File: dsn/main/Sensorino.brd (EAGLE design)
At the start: 100 x 80 mm, 45 parts, among them IC1 LDO3V3

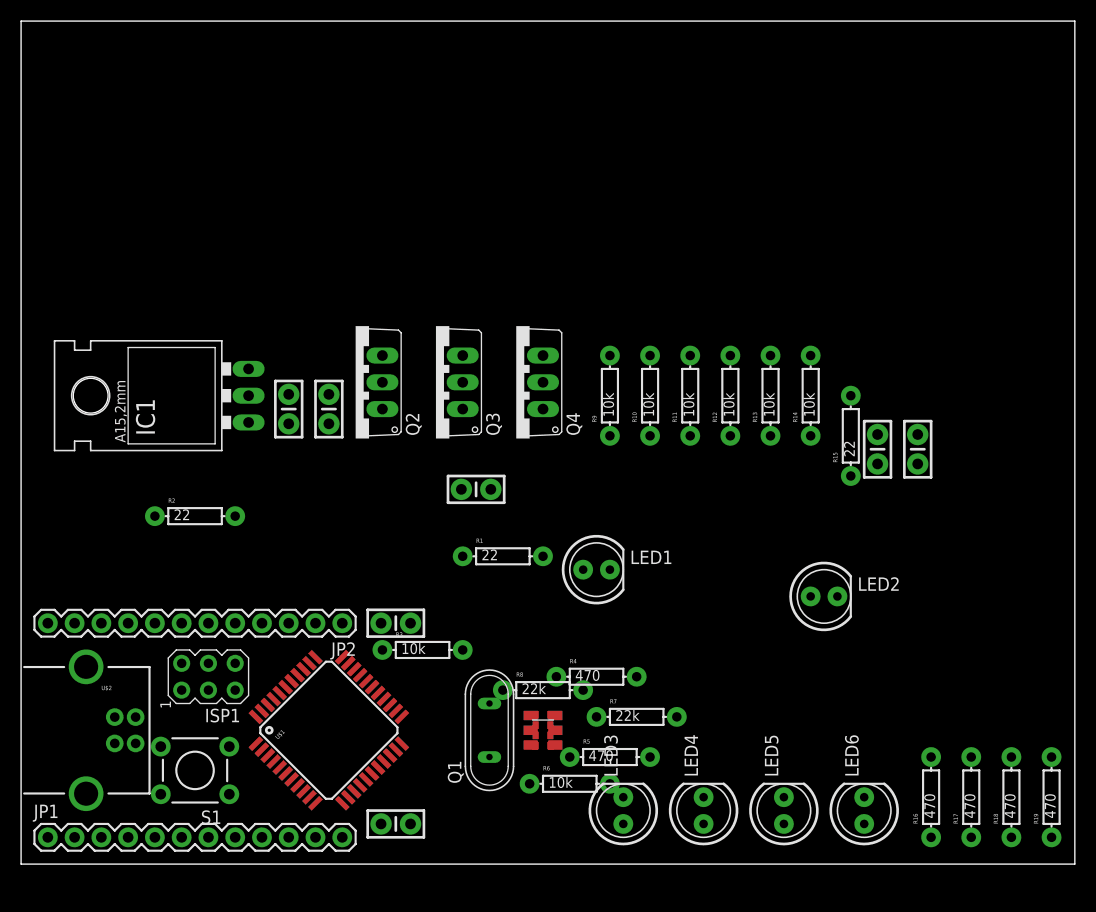
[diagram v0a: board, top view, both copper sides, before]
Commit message: Added PTH render
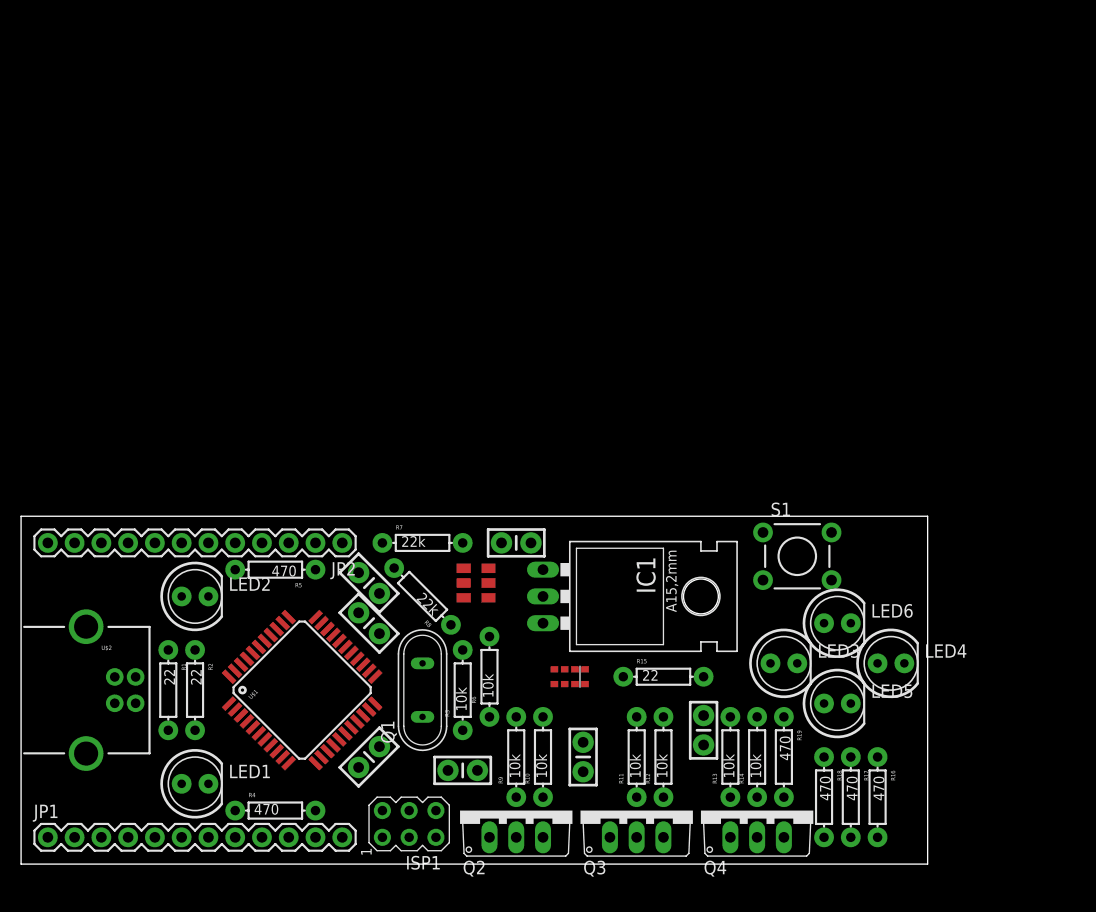
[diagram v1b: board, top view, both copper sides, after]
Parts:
- Q1: value (none) -> 16Mhz
- moved S1 60.7 mm to (73.7, 29.2), turned to 0 degrees
- moved LED2 59.7 mm to (16.5, 25.4)
- moved Q4 46.6 mm to (69.8, 5.08), turned to 0 degrees
- moved Q3 44.9 mm to (58.4, 5.08), turned to 0 degrees
- moved Q2 43.4 mm to (47.0, 5.08), turned to 0 degrees
- moved LED1 43.2 mm to (16.5, 7.62)
- moved C7 43.1 mm to (53.3, 10.2), turned to 270 degrees
- moved IC1 40.3 mm to (53.3, 25.4), turned to 270 degrees
- moved C5 36.6 mm to (41.9, 8.89), turned to 180 degrees
- moved R5 36.4 mm to (24.1, 27.9), turned to 180 degrees
- moved R10 35.8 mm to (49.5, 10.2)
- moved R9 35.4 mm to (47.0, 10.2)
- moved R12 34.9 mm to (61.0, 10.2)
- moved R11 34.7 mm to (58.4, 10.2)
- moved R14 34.7 mm to (69.8, 10.2)
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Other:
- board size 100 x 80 mm -> 86 x 33 mm

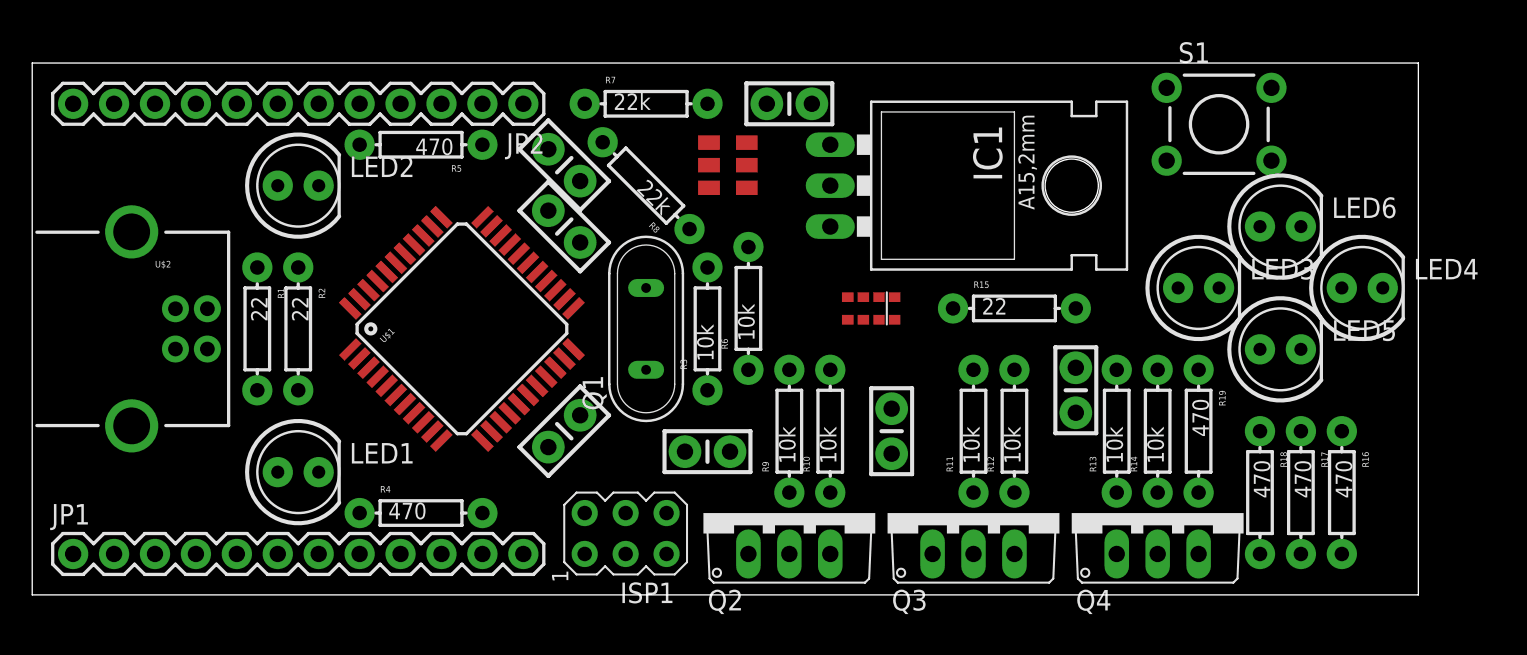
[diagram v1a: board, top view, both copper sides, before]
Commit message: Mosfet changed to a more-acceptable model
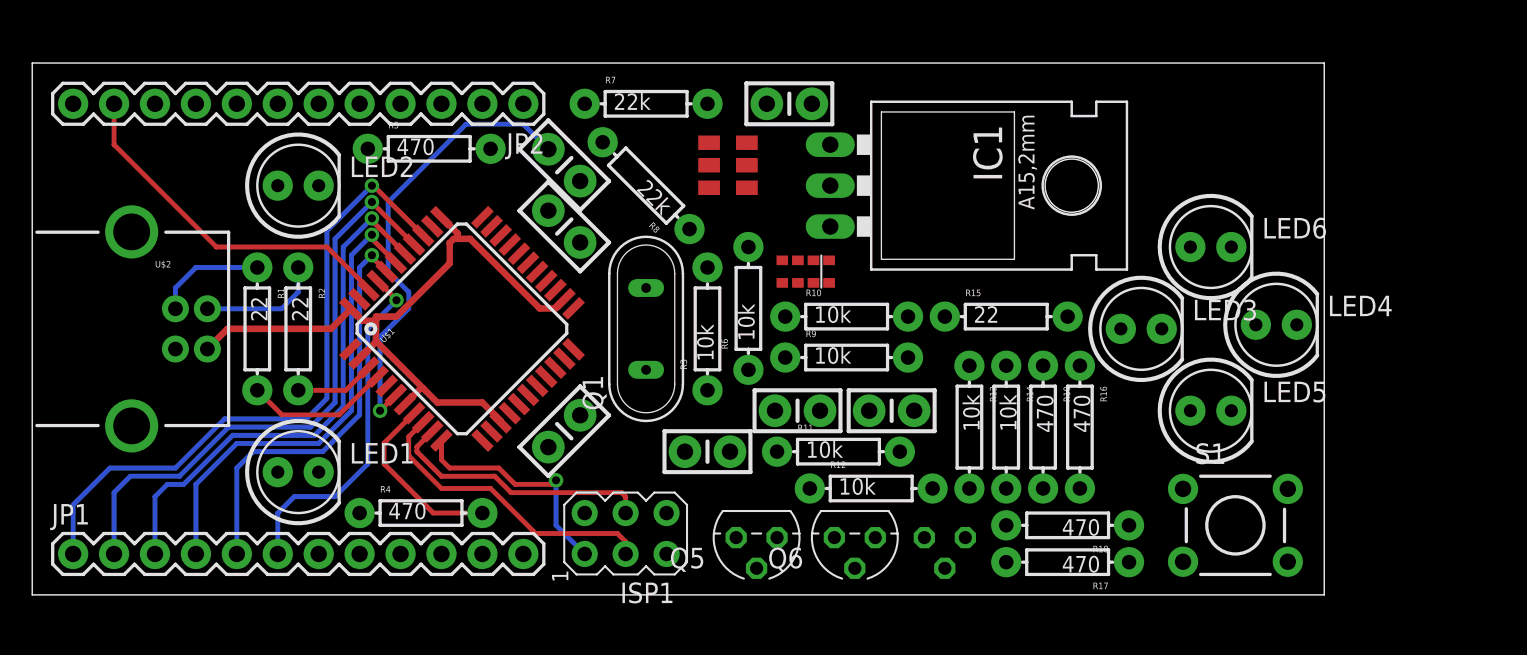
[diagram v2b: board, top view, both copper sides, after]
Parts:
- removed Q2, Q3, Q4: (no value), adafruit:TO220V
- added Q5, Q6, Q7: BSS101, transistor-fet:TO92
- moved S1 24.9 mm to (74.7, 4.32)
- moved R16 16.8 mm to (65.0, 10.4)
- moved R17 15.1 mm to (64.3, 2.03), turned to 180 degrees
- moved R18 12.1 mm to (64.3, 4.32), turned to 180 degrees
- moved C6 11.5 mm to (53.3, 11.4), turned to 180 degrees
- moved R19 9.66 mm to (62.7, 10.4)
- moved R12 9.57 mm to (52.1, 6.60), turned to 0 degrees
- moved R14 9.40 mm to (60.5, 10.4), turned to 270 degrees
- moved R13 9.15 mm to (58.2, 10.4), turned to 270 degrees
- moved R11 8.48 mm to (50.0, 8.89), turned to 0 degrees
- moved R10 7.18 mm to (50.5, 17.3), turned to 0 degrees
- moved C7 5.98 mm to (47.5, 11.4), turned to 180 degrees
- moved LED4 5.80 mm to (77.2, 16.8)
- moved R9 5.79 mm to (50.5, 14.7), turned to 0 degrees
- moved LED5 5.76 mm to (73.2, 11.4)
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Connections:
- net 3V3_PWR: now also Q5.2, Q6.2, Q7.2; no longer Q2.1, Q3.1, Q4.1
- net A1: now also Q5.1; no longer Q2.3
- net A2: now also Q6.1; no longer Q4.3
- net A3: now also Q7.1; no longer Q3.3
- net B1: now also Q5.3; no longer Q2.2
- net B2: now also Q6.3; no longer Q4.2
- net B3: now also Q7.3; no longer Q3.2
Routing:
- net 5V: track 0.00 -> 44.5 mm
- net N$13: track 0.00 -> 40.4 mm, vias 0 -> 1
- net N$14: track 0.00 -> 37.0 mm, vias 0 -> 1
- net N$15: track 0.00 -> 33.0 mm, vias 0 -> 1
- net N$16: track 0.00 -> 29.7 mm, vias 0 -> 1
- net N$6: track 0.00 -> 28.2 mm, vias 0 -> 1
- net N$17: track 0.00 -> 26.0 mm, vias 0 -> 1
- net AREF_SIG: track 0.00 -> 22.1 mm
- net N$18: track 0.00 -> 22.0 mm, vias 0 -> 1
- net SCK_SIG: track 0.00 -> 18.9 mm
- net MOSI_SIG: track 0.00 -> 16.8 mm
- net MISO_SIG: track 0.00 -> 14.4 mm, vias 0 -> 1
- net RXL_SIG: track 0.00 -> 11.3 mm
- net N$2: track 0.00 -> 9.08 mm
- net N$4: track 0.00 -> 7.59 mm
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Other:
- board size 86 x 33 mm -> 80.2 x 33 mm

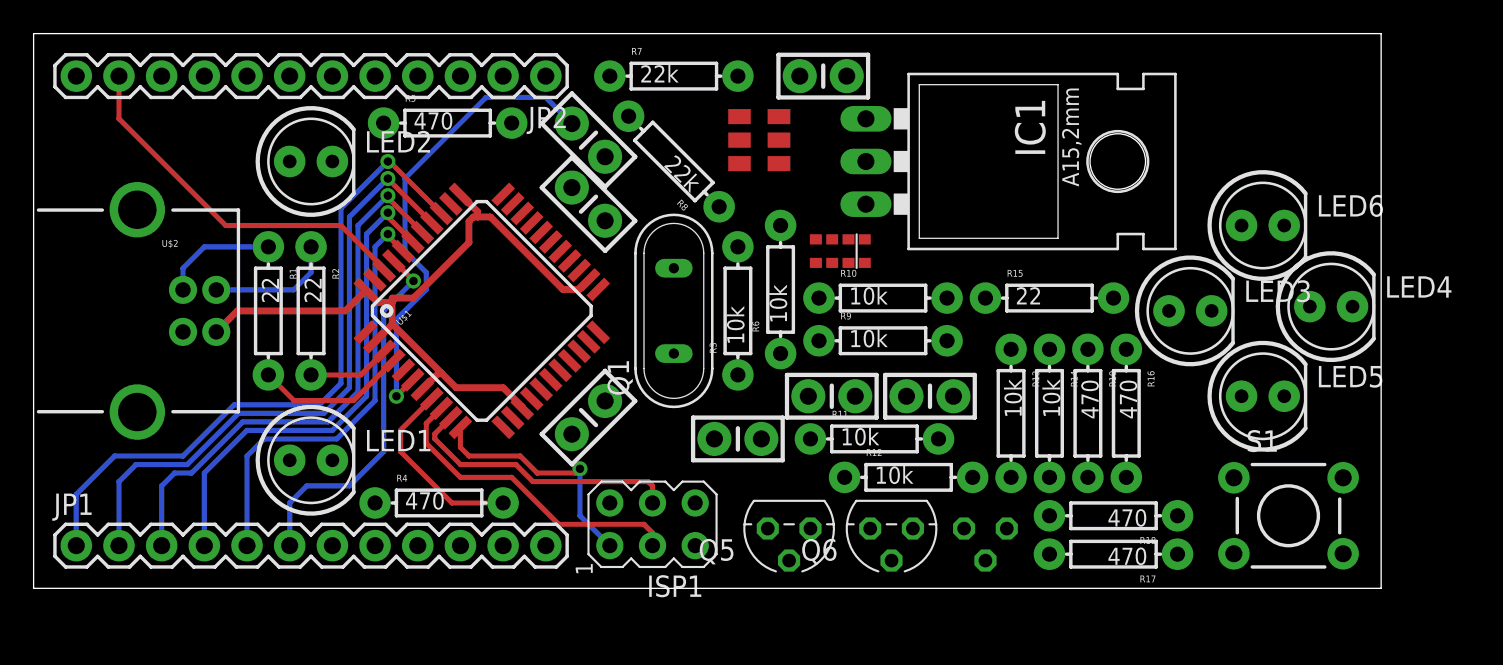
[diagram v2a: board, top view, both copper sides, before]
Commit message: Modified PTH PCB Layout
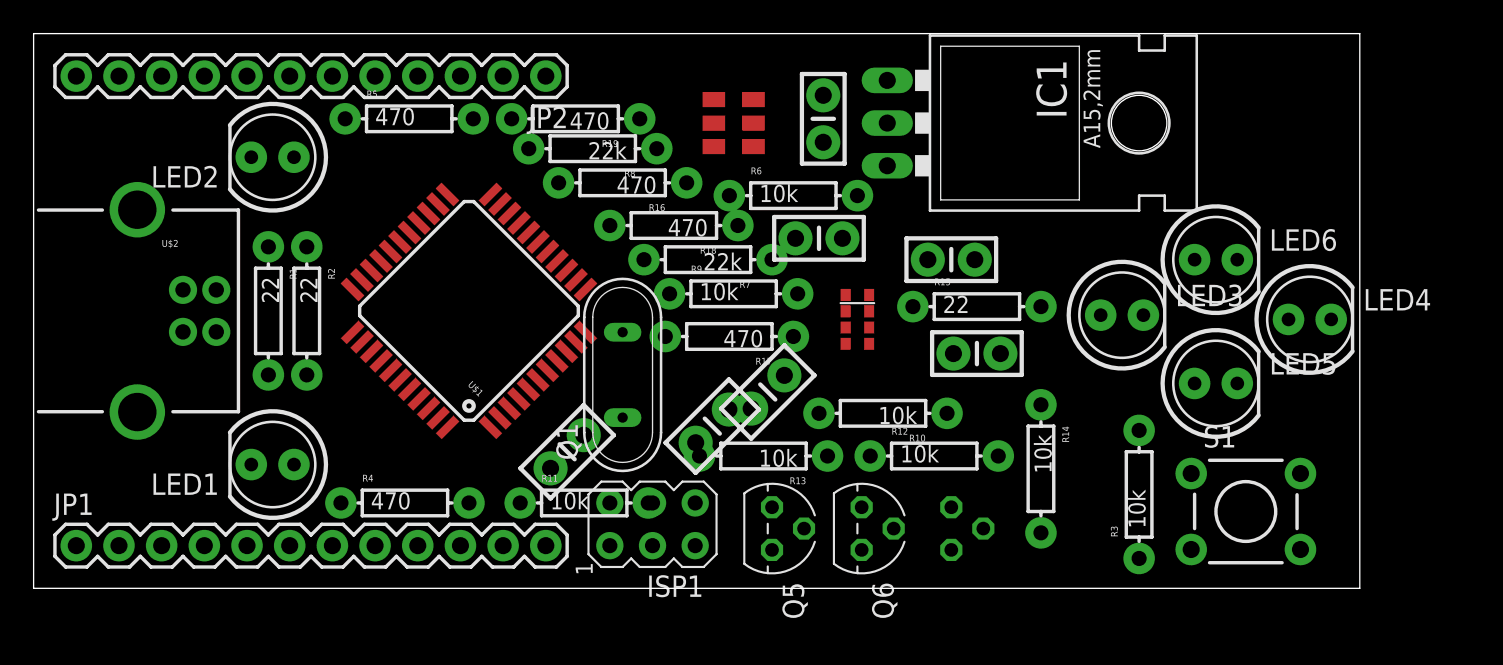
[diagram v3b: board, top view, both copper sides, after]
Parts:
- moved R19 35.2 mm to (32.3, 27.9), turned to 180 degrees
- moved R16 33.0 mm to (35.1, 24.1), turned to 180 degrees
- moved R18 31.3 mm to (38.1, 21.6)
- moved R17 26.3 mm to (41.4, 15.0)
- moved R3 26.3 mm to (65.8, 5.59)
- moved C1 18.5 mm to (40.4, 9.65), turned to 225 degrees
- moved R11 17.7 mm to (32.8, 5.08)
- moved C5 16.6 mm to (54.6, 19.6)
- moved C3 15.5 mm to (43.7, 11.7), turned to 45 degrees
- moved R13 14.9 mm to (43.4, 7.87), turned to 180 degrees
- moved R7 11.1 mm to (40.1, 19.6), turned to 180 degrees
- moved C7 9.43 mm to (46.7, 20.8)
- moved R9 9.32 mm to (41.7, 17.5)
- moved R10 6.86 mm to (50.5, 10.4), turned to 180 degrees
- moved R6 5.64 mm to (45.2, 23.4), turned to 0 degrees
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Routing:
- net 5V: track 44.5 -> 0.00 mm
- net N$13: track 40.4 -> 0.00 mm, vias 1 -> 0
- net N$14: track 37.0 -> 0.00 mm, vias 1 -> 0
- net N$15: track 33.0 -> 0.00 mm, vias 1 -> 0
- net N$16: track 29.7 -> 0.00 mm, vias 1 -> 0
- net N$6: track 28.2 -> 0.00 mm, vias 1 -> 0
- net N$17: track 26.0 -> 0.00 mm, vias 1 -> 0
- net AREF_SIG: track 22.1 -> 0.00 mm
- net N$18: track 22.0 -> 0.00 mm, vias 1 -> 0
- net SCK_SIG: track 18.9 -> 0.00 mm
- net MOSI_SIG: track 16.8 -> 0.00 mm
- net MISO_SIG: track 14.4 -> 0.00 mm, vias 1 -> 0
- net RXL_SIG: track 11.3 -> 0.00 mm
- net N$2: track 9.08 -> 0.00 mm
- net N$4: track 7.59 -> 0.00 mm
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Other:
- board size 80.2 x 33 mm -> 78.9 x 33 mm

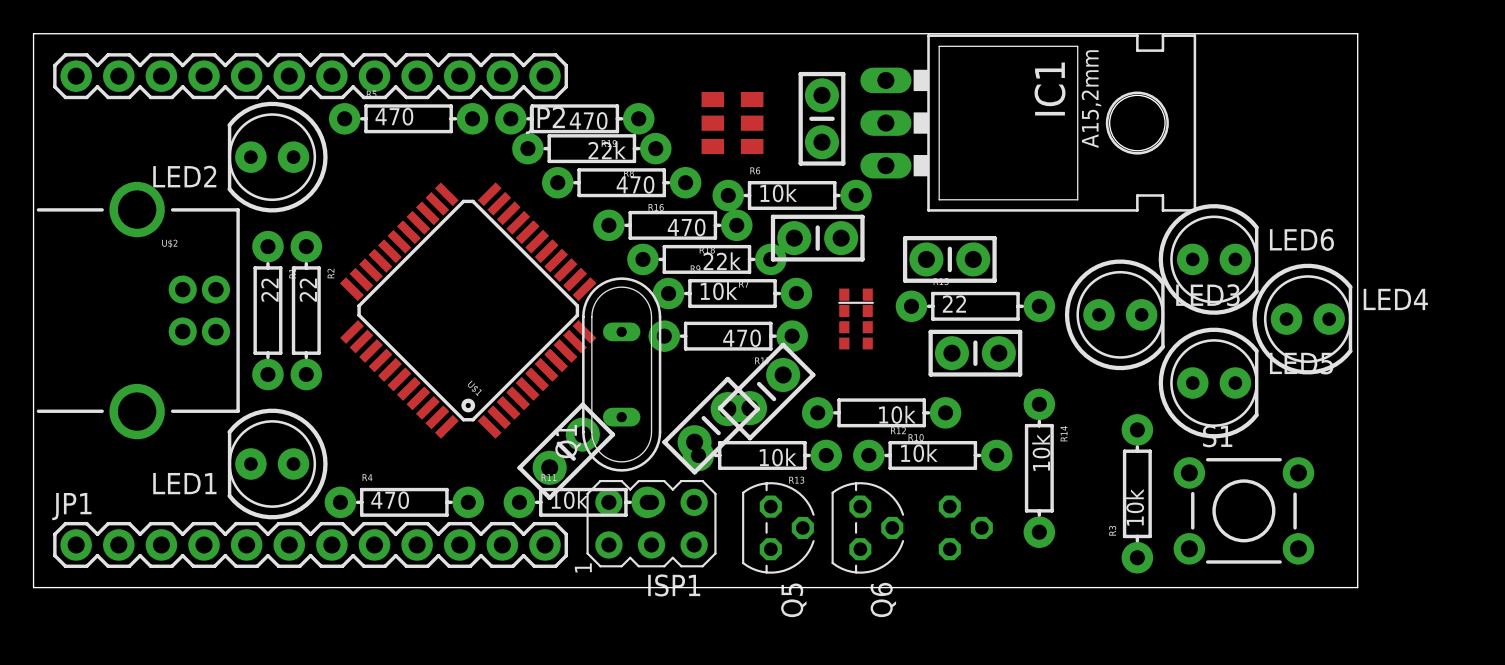
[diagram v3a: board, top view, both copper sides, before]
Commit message: Added SMD version
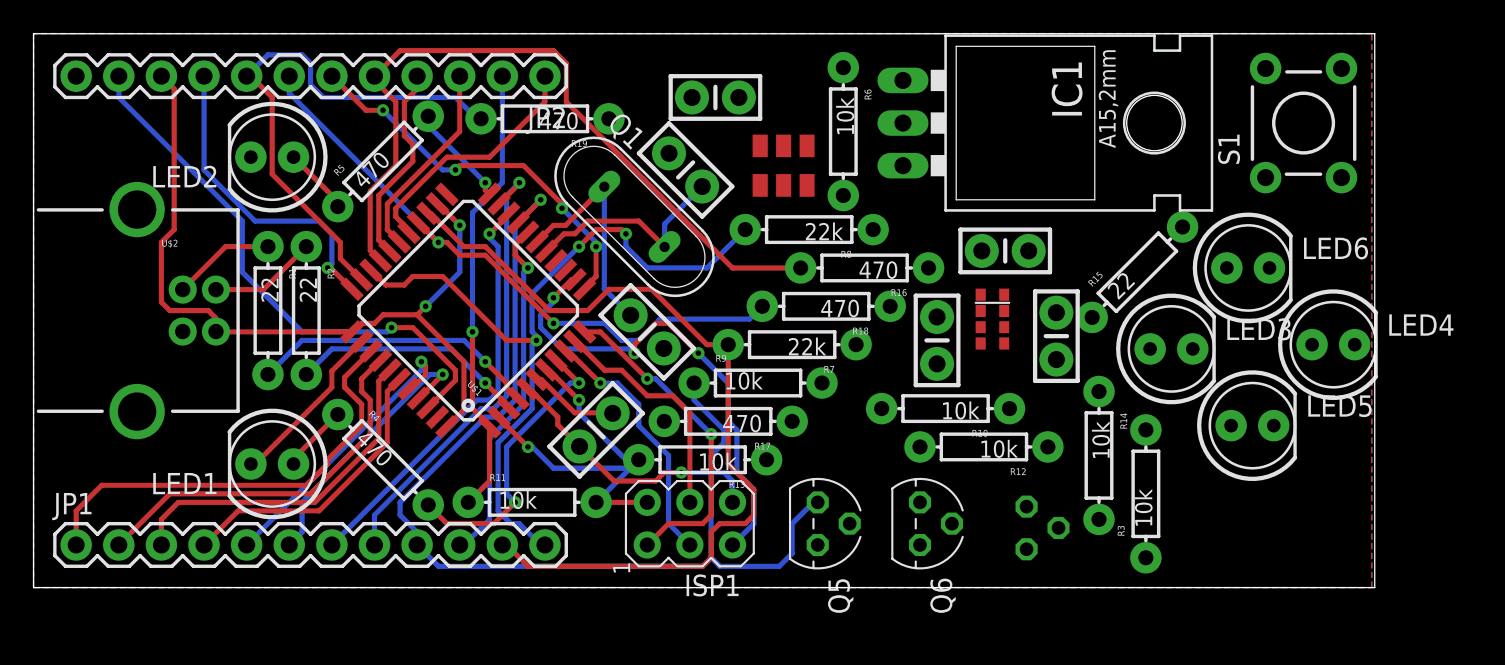
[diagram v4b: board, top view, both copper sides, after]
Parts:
- moved S1 23.4 mm to (75.7, 27.7), turned to 90 degrees
- moved R16 15.3 mm to (49.5, 19.1)
- moved C3 14.1 mm to (38.9, 24.9), turned to 135 degrees
- moved R8 13.8 mm to (46.2, 21.3)
- moved R18 10.3 mm to (47.2, 16.8)
- moved R15 9.86 mm to (65.8, 18.8), turned to 45 degrees
- moved Q1 9.43 mm to (35.8, 22.1), turned to 315 degrees
- moved C7 9.37 mm to (53.8, 14.7), turned to 270 degrees
- moved C2 8.59 mm to (36.6, 15.2), turned to 315 degrees
- moved U$4 8.13 mm to (57.1, 16.0)
- moved R7 7.18 mm to (45.2, 14.5)
- moved C1 6.86 mm to (33.5, 9.40), turned to 45 degrees
- moved C4 6.48 mm to (40.6, 29.2), turned to 0 degrees
- moved R9 5.55 mm to (43.2, 12.2)
- moved R17 5.08 mm to (41.4, 9.91)
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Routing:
- net 5V: track 0.00 -> 72.1 mm, vias 0 -> 4
- net B1: track 0.00 -> 65.8 mm, vias 0 -> 1
- net S1_SIG: track 0.00 -> 50.7 mm
- net S2_SIG: track 0.00 -> 46.3 mm, vias 0 -> 3
- net LED1_SIG: track 0.00 -> 45.1 mm
- net LED3_SIG: track 0.00 -> 37.8 mm, vias 0 -> 2
- net AREF_SIG: track 0.00 -> 33.0 mm, vias 0 -> 1
- net LED4_SIG: track 0.00 -> 31.9 mm
- net RST_SIG: track 0.00 -> 28.9 mm, vias 0 -> 3
- net N$20: track 0.00 -> 27.4 mm, vias 0 -> 1
- net B3: track 0.00 -> 27.1 mm, vias 0 -> 1
- net N$13: track 0.00 -> 26.8 mm
- net GND: track 0.00 -> 26.6 mm, vias 0 -> 1
- net N$19: track 0.00 -> 25.0 mm, vias 0 -> 1
- net LED2_SIG: track 0.00 -> 23.3 mm, vias 0 -> 4
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- added copper zone on layer 1, net GND
- added copper zone on layer 16, net GND
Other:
- board size 78.9 x 33 mm -> 79.9 x 33 mm
